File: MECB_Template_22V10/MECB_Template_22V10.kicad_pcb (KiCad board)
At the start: 2 copper layers, 99.8 x 99.8 mm, 6 parts, among them J1 MECB_64AC, U1 ATF22V10C-15PU

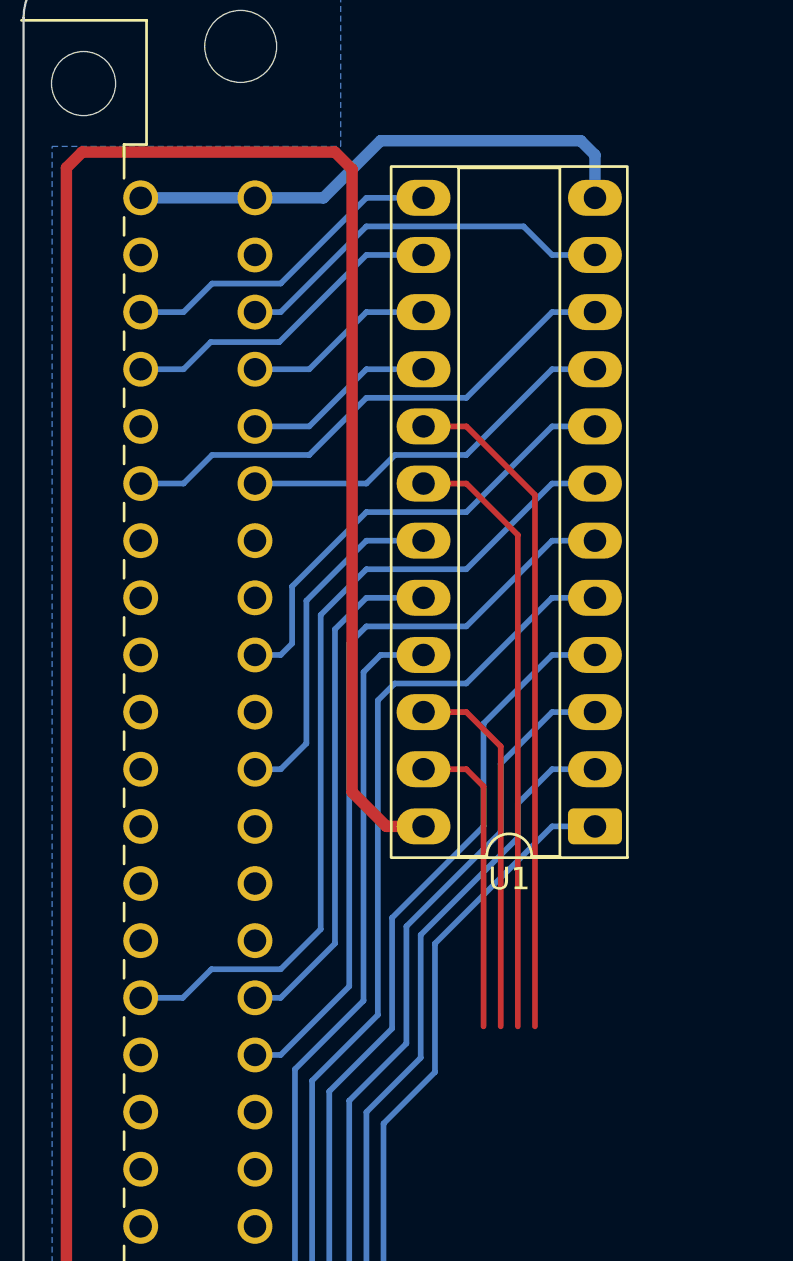
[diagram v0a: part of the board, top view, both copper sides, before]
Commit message: Update MECB KiCAD Templates. Include 220nf bypass capacitor. Re-route tracks based on new capacitor positioning. Update 3D images to be new blue colouring. Correct earth zone inner corner rounding.
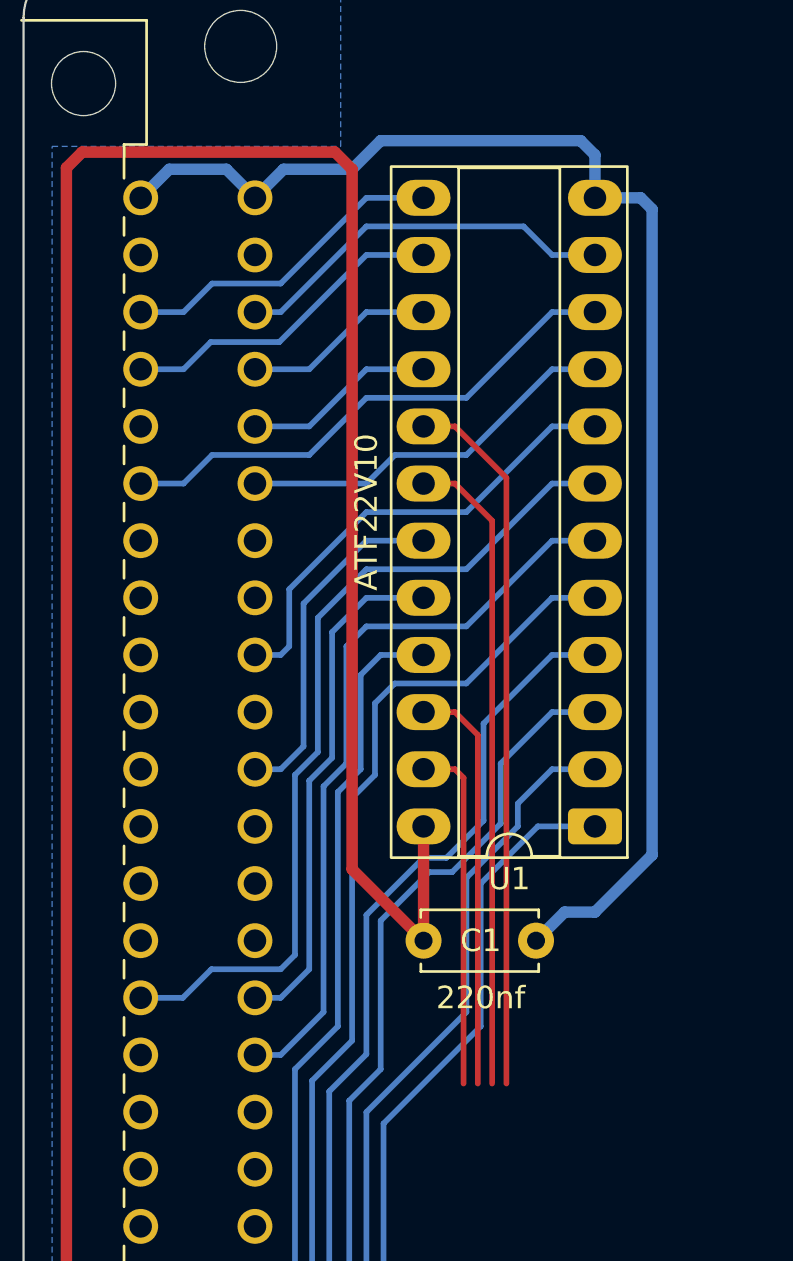
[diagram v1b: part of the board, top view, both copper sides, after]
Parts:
- added C1: 0.22uf, Capacitor_THT:C_Disc_D5.0mm_W2.5mm_P5.00mm, F.Cu at (114.3, 90.2)
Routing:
- net GND: track 23.4 -> 62.7 mm
- net +5V: track 132.9 -> 142.1 mm
- net CS0: track 13.7 -> 15.5 mm
- net CS1: track 16.5 -> 18.3 mm
- net CS2: track 27.0 -> 28.8 mm
- net CS3: track 29.8 -> 31.6 mm
- net /ECB_A5: track 53.0 -> 53.6 mm
- net /ECB_A8: track 46.1 -> 46.7 mm
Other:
- board text added: "220nf"
- board text added: "ATF22V10"
